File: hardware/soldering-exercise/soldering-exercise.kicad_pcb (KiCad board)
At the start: 2 copper layers, 18 parts, among them J1 SAO v1.69bis addon, U1 NE555P

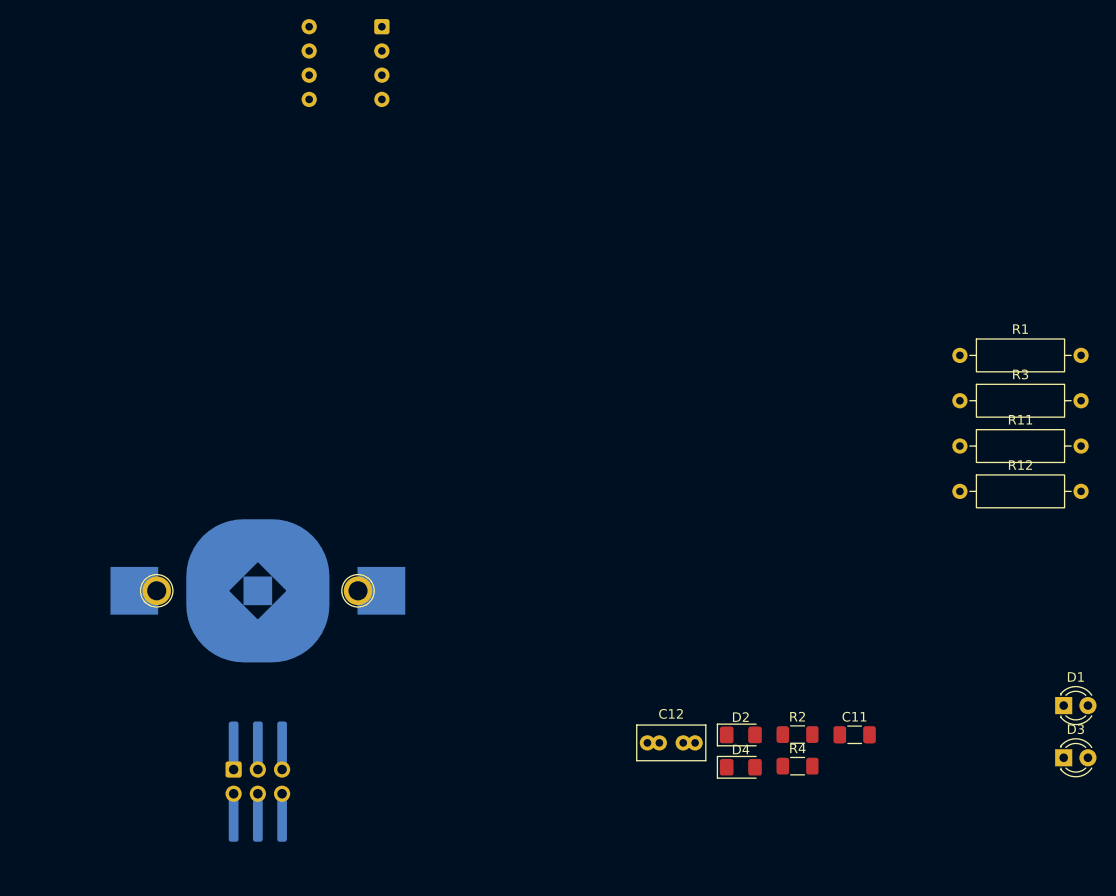
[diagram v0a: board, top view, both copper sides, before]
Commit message: duplicate THT to SMD, layout board
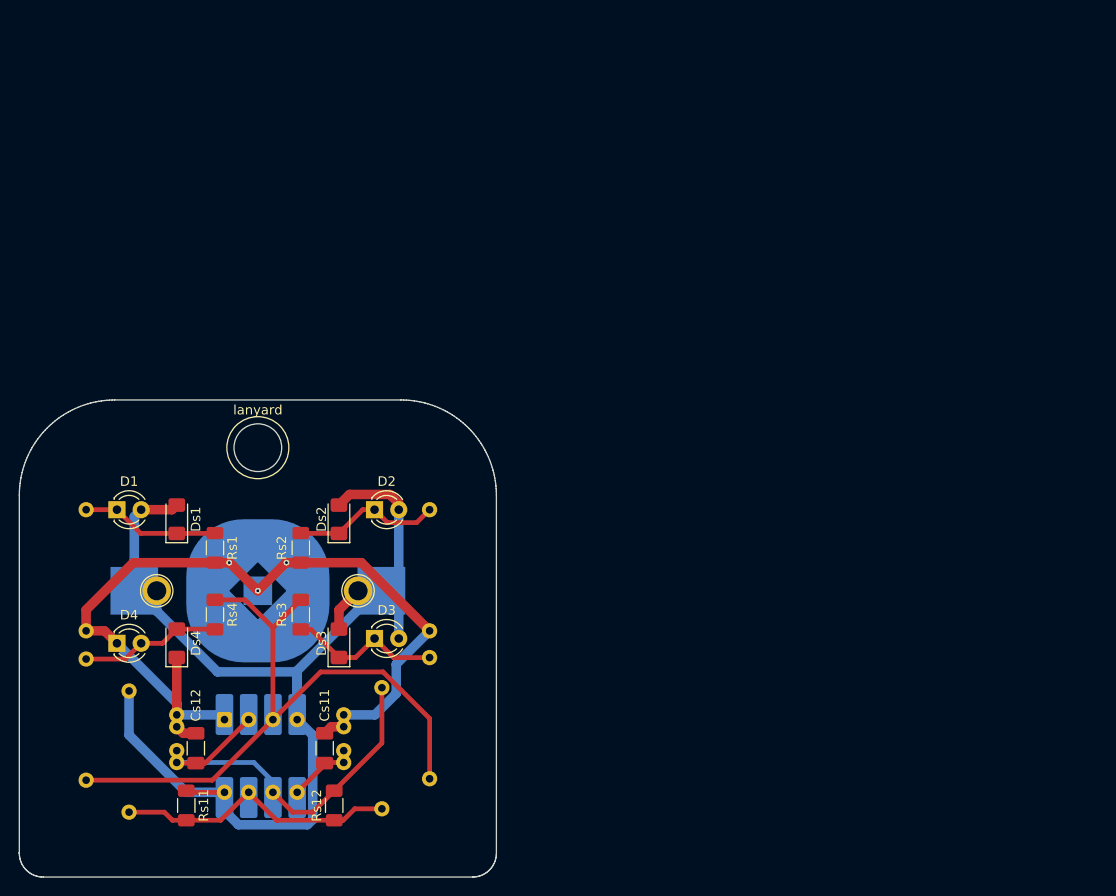
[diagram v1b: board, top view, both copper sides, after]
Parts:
- removed J1: SAO v1.69bis addon, Connector_IDC:IDC-Header_2x03_P2.54mm_Vertical
- removed J1: SAO v1.69bis addon, Connector_IDC:IDC-Header_2x03_P2.54mm_Vertical_SMD
- added Cs11: C, Capacitor_SMD:C_1206_3216Metric_Pad1.33x1.80mm_HandSolder, F.Cu at (107.0, 116.5)
- added Cs12: C, Capacitor_SMD:C_1206_3216Metric_Pad1.33x1.80mm_HandSolder, F.Cu at (93.5, 116.5)
- added Ds1: LED, LED_SMD:LED_1206_3216Metric_Pad1.42x1.75mm_HandSolder, F.Cu at (91.5, 92.5)
- added Ds2: LED, LED_SMD:LED_1206_3216Metric_Pad1.42x1.75mm_HandSolder, F.Cu at (108.5, 92.5)
- added Ds3: LED, LED_SMD:LED_1206_3216Metric_Pad1.42x1.75mm_HandSolder, F.Cu at (108.5, 105.5)
- added Ds4: LED, LED_SMD:LED_1206_3216Metric_Pad1.42x1.75mm_HandSolder, F.Cu at (91.5, 105.5)
- added Rs1: R, Resistor_SMD:R_1206_3216Metric_Pad1.30x1.75mm_HandSolder, F.Cu at (95.5, 95.5)
- added Rs11: R, Resistor_SMD:R_1206_3216Metric_Pad1.30x1.75mm_HandSolder, F.Cu at (92.5, 122.5)
- added Rs12: R, Resistor_SMD:R_1206_3216Metric_Pad1.30x1.75mm_HandSolder, F.Cu at (108.0, 122.5)
- added Rs2: R, Resistor_SMD:R_1206_3216Metric_Pad1.30x1.75mm_HandSolder, F.Cu at (104.5, 95.5)
- added Rs3: R, Resistor_SMD:R_1206_3216Metric_Pad1.30x1.75mm_HandSolder, F.Cu at (104.5, 102.5)
- added Rs4: R, Resistor_SMD:R_1206_3216Metric_Pad1.30x1.75mm_HandSolder, F.Cu at (95.5, 102.5)
- added Us2: NE555P, Package_SO:SOP-8_6.605x9.655mm_P2.54mm, B.Cu at (100.3, 117.3)
- added lanyard: TestPoint_Plated_Hole_D5.0mm, TestPoint:TestPoint_Plated_Hole_D5.0mm, F.Cu at (100.0, 85.0)
- C11: footprint Capacitor_SMD:C_1206_3216Metric_Pad1.33x1.80mm_HandSolder -> Capacitor_THT:C_Rect_L7.0mm_W3.5mm_P2.50mm_P5.00mm; moved to B.Cu
- C12, R1, R11, R12, R3: moved to B.Cu
- D2, D4: footprint LED_SMD:LED_1206_3216Metric_Pad1.42x1.75mm_HandSolder -> LED_THT:LED_D3.0mm_Clear
- R2, R4: footprint Resistor_SMD:R_1206_3216Metric_Pad1.30x1.75mm_HandSolder -> Resistor_THT:R_Axial_DIN0309_L9.0mm_D3.2mm_P12.70mm_Horizontal; moved to B.Cu
- moved D1 101.3 mm to (85.2, 91.5)
- moved R1 93.0 mm to (82.0, 91.5), turned to -90 degrees
- moved R11 90.8 mm to (86.5, 110.5), turned to -90 degrees
- moved R4 74.6 mm to (82.0, 119.8), turned to 90 degrees
- moved U1 74.5 mm to (96.5, 113.5), turned to -90 degrees
- moved D3 73.3 mm to (112.2, 105.0)
- moved R12 69.1 mm to (113.0, 122.8), turned to 90 degrees
- moved D4 66.7 mm to (85.2, 105.5)
- moved R3 61.8 mm to (118.0, 107.0), turned to -90 degrees
- moved C11 53.6 mm to (109.0, 118.0), turned to 90 degrees
- moved C12 49.4 mm to (91.5, 118.0), turned to 90 degrees
- moved R2 45.2 mm to (118.0, 91.5), turned to -90 degrees
- moved D2 45.1 mm to (112.2, 91.5)
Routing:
- net +3V3: track 0.00 -> 122.6 mm
- net GND: track 0.00 -> 89.8 mm, vias 0 -> 3
- net Net-(U1-Q): track 0.00 -> 70.1 mm
- net Net-(U1-THR): track 0.00 -> 42.6 mm
- net Net-(U1-DIS): track 0.00 -> 29.8 mm
- net Net-(D3-K): track 0.00 -> 16.4 mm
- net Net-(D2-K): track 0.00 -> 15.7 mm
- net Net-(D4-A): track 0.00 -> 14.8 mm
- net Net-(D1-K): track 0.00 -> 14.5 mm
- net Net-(U1-CV): track 0.00 -> 6.28 mm
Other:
- board outline added: 50 x 50 mm

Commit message: added PhreakNIC logo
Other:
- board text added: "PhreakNIC 26"
- board text added: "soldering workshop"
